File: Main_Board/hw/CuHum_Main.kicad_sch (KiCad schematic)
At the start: 50 parts, among them J1 Barrel_Jack_Switch_Pin3Ring, J101 Conn_01x07, J102 Conn_01x07, J103 Conn_01x07, J104 Conn_01x07, J105 Conn_01x07, J106 Conn_01x07, J107 Conn_01x07, J108 Conn_01x07, J109 Conn_01x07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

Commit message: Finish main board layout
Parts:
- J2: footprint CuHum_Main_footprints:TestPoints_1x04_P2.0 -> CuHum_Main_footprints:TestPoints_1x04_P2.54
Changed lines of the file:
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@@
       (effects (font (size 1.27 1.27)) (justify left) hide)
     )
-    (property "Footprint" "CuHum_Main_footprints:TestPoints_1x04_P2.0" (at 14.605 111.125 0)
+    (property "Footprint" "CuHum_Main_footprints:TestPoints_1x04_P2.54" (at 14.605 111.125 0)
       (effects (font (size 1.27 1.27)) hide)
     )

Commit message: (WIP) Main board layout & routing
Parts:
- J101, J102, J103, J104, J105, J106, J107, J108, J109, J110, J111, J112, J113, J114, J115: footprint Connector_PinHeader_2.54mm:PinHeader_1x07_P2.54mm_Vertical -> CuHum_Main_footprints:Unit_1x07_P2.54
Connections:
- net UNIT_CAP_01: now also U6.19 (LED7/ELE11); no longer U5.8 (ELE0)
- net UNIT_CAP_02: now also U5.10 (ELE2); no longer U5.9 (ELE1)
- net UNIT_CAP_03: now also U5.13 (LED1/ELE5); no longer U5.10 (ELE2)
- net UNIT_CAP_04: now also U5.18 (LED6/ELE10); no longer U5.11 (ELE3)
- net UNIT_CAP_05: now also U6.9 (ELE1); no longer U5.12 (LED0/ELE4)
- net UNIT_CAP_06: now also U6.13 (LED1/ELE5); no longer U5.13 (LED1/ELE5)
- net UNIT_CAP_07: now also U6.17 (LED5/ELE9); no longer U5.14 (LED2/ELE6)
- net UNIT_CAP_08: now also U5.9 (ELE1); no longer U5.15 (LED3/ELE7)
- net UNIT_CAP_09: now also U5.11 (ELE3); no longer U5.16 (LED4/ELE8)
- net UNIT_CAP_10: now also U5.16 (LED4/ELE8); no longer U5.17 (LED5/ELE9)
- net UNIT_CAP_11: now also U5.19 (LED7/ELE11); no longer U5.18 (LED6/ELE10)
- net UNIT_CAP_12: now also U6.10 (ELE2); no longer U5.19 (LED7/ELE11)
- net UNIT_CAP_13: now also U6.15 (LED3/ELE7); no longer U6.8 (ELE0)
- net UNIT_CAP_14: now also U6.18 (LED6/ELE10); no longer U6.9 (ELE1)
- net UNIT_CAP_15: now also U5.8 (ELE0); no longer U6.10 (ELE2)

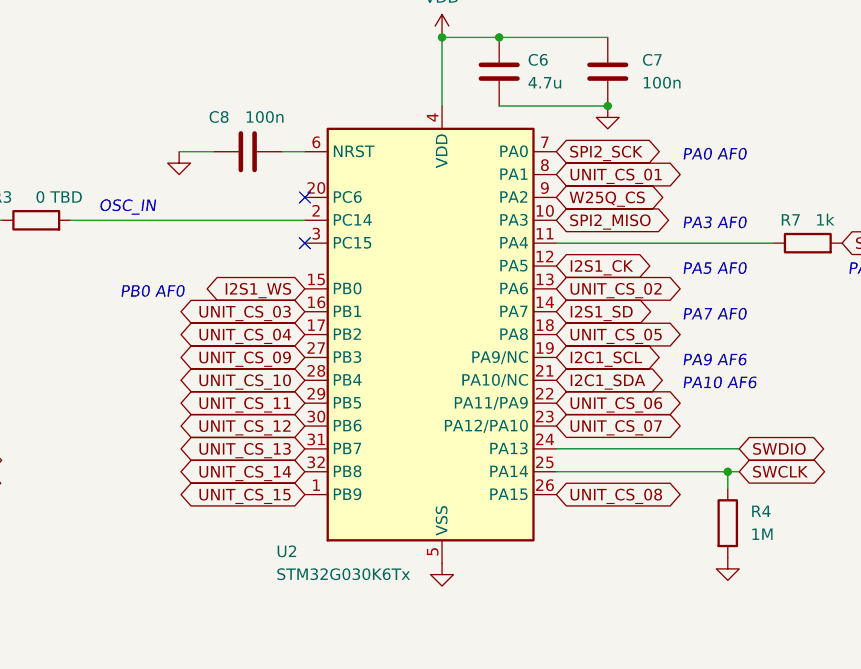
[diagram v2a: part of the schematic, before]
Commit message: Finish main board routing
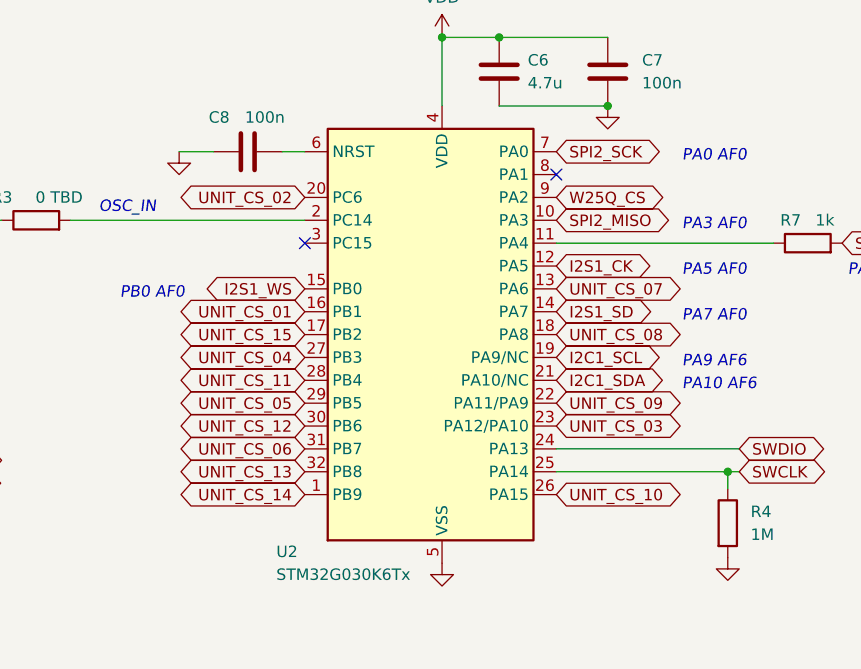
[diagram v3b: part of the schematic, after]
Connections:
- net UNIT_CS_01: now also U2.16 (PB1); no longer U2.8 (PA1)
- net UNIT_CS_02: now also U2.20 (PC6); no longer U2.13 (PA6)
- net UNIT_CS_03: now also U2.23 (PA12/PA10); no longer U2.16 (PB1)
- net UNIT_CS_04: now also U2.27 (PB3); no longer U2.17 (PB2)
- net UNIT_CS_05: now also U2.29 (PB5); no longer U2.18 (PA8)
- net UNIT_CS_06: now also U2.31 (PB7); no longer U2.22 (PA11/PA9)
- net UNIT_CS_07: now also U2.13 (PA6); no longer U2.23 (PA12/PA10)
- net UNIT_CS_08: now also U2.18 (PA8); no longer U2.26 (PA15)
- net UNIT_CS_09: now also U2.22 (PA11/PA9); no longer U2.27 (PB3)
- net UNIT_CS_10: now also U2.26 (PA15); no longer U2.28 (PB4)
- net UNIT_CS_11: now also U2.28 (PB4); no longer U2.29 (PB5)
- net UNIT_CS_13: now also U2.32 (PB8); no longer U2.31 (PB7)
- net UNIT_CS_14: now also U2.1 (PB9); no longer U2.32 (PB8)
- net UNIT_CS_15: now also U2.17 (PB2); no longer U2.1 (PB9)
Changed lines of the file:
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@@
   (no_connect (at 157.48 79.375))
   (no_connect (at 43.815 164.465))
+  (no_connect (at 90.805 81.915))
   (no_connect (at 62.865 89.535))
   (no_connect (at 250.19 88.9))
   (no_connect (at 137.795 161.925))
-  (no_connect (at 62.865 84.455))
   (no_connect (at 181.61 102.235))
   (no_connect (at 137.795 169.545))
@@
     )
   )
-  (global_label "UNIT_CS_01" (shape bidirectional) (at 90.805 81.915 0) (fields_autoplaced)
-    (effects (font (size 1.27 1.27)) (justify left))
-    (property "Intersheetrefs" "${INTERSHEET_REFS}" (at 105.9686 81.915 0)
-      (effects (font (size 1.27 1.27)) (justify left) hide)
-    )
-  )
   (global_label "UNIT_CAP_01" (shape bidirectional) (at 137.795 182.245 0) (fields_autoplaced)
     (effects (font (size 1.27 1.27)) (justify left))
@@
     )
   )
-  (global_label "UNIT_CS_11" (shape bidirectional) (at 62.865 107.315 180) (fields_autoplaced)
+  (global_label "UNIT_CS_05" (shape bidirectional) (at 62.865 107.315 180) (fields_autoplaced)
     (effects (font (size 1.27 1.27)) (justify right))
     (property "Intersheetrefs" "${INTERSHEET_REFS}" (at 47.7014 107.315 0)
@@
     )
   )
-  (global_label "UNIT_CS_04" (shape bidirectional) (at 62.865 99.695 180) (fields_autoplaced)
+  (global_label "UNIT_CS_15" (shape bidirectional) (at 62.865 99.695 180) (fields_autoplaced)
     (effects (font (size 1.27 1.27)) (justify right))
     (property "Intersheetrefs" "${INTERSHEET_REFS}" (at 47.7014 99.695 0)
@@
     )
   )
-  (global_label "UNIT_CS_14" (shape bidirectional) (at 62.865 114.935 180) (fields_autoplaced)
+  (global_label "UNIT_CS_13" (shape bidirectional) (at 62.865 114.935 180) (fields_autoplaced)
     (effects (font (size 1.27 1.27)) (justify right))
     (property "Intersheetrefs" "${INTERSHEET_REFS}" (at 47.7014 114.935 0)
@@
     )
   )
-  (global_label "UNIT_CS_09" (shape bidirectional) (at 62.865 102.235 180) (fields_autoplaced)
+  (global_label "UNIT_CS_04" (shape bidirectional) (at 62.865 102.235 180) (fields_autoplaced)
     (effects (font (size 1.27 1.27)) (justify right))
     (property "Intersheetrefs" "${INTERSHEET_REFS}" (at 47.7014 102.235 0)
@@
     )
   )
-  (global_label "UNIT_CS_13" (shape bidirectional) (at 62.865 112.395 180) (fields_autoplaced)
+  (global_label "UNIT_CS_06" (shape bidirectional) (at 62.865 112.395 180) (fields_autoplaced)
     (effects (font (size 1.27 1.27)) (justify right))
     (property "Intersheetrefs" "${INTERSHEET_REFS}" (at 47.7014 112.395 0)
@@
     )
   )
-  (global_label "UNIT_CS_05" (shape bidirectional) (at 90.805 99.695 0) (fields_autoplaced)
+  (global_label "UNIT_CS_08" (shape bidirectional) (at 90.805 99.695 0) (fields_autoplaced)
     (effects (font (size 1.27 1.27)) (justify left))
     (property "Intersheetrefs" "${INTERSHEET_REFS}" (at 105.9686 99.695 0)
@@
     )
   )
-  (global_label "UNIT_CS_15" (shape bidirectional) (at 62.865 117.475 180) (fields_autoplaced)
+  (global_label "UNIT_CS_14" (shape bidirectional) (at 62.865 117.475 180) (fields_autoplaced)
     (effects (font (size 1.27 1.27)) (justify right))
     (property "Intersheetrefs" "${INTERSHEET_REFS}" (at 47.7014 117.475 0)
@@
     )
   )
-  (global_label "UNIT_CS_03" (shape bidirectional) (at 62.865 97.155 180) (fields_autoplaced)
+  (global_label "UNIT_CS_01" (shape bidirectional) (at 62.865 97.155 180) (fields_autoplaced)
     (effects (font (size 1.27 1.27)) (justify right))
     (property "Intersheetrefs" "${INTERSHEET_REFS}" (at 47.7014 97.155 0)
@@
     )
   )
-  (global_label "UNIT_CS_10" (shape bidirectional) (at 62.865 104.775 180) (fields_autoplaced)
+  (global_label "UNIT_CS_11" (shape bidirectional) (at 62.865 104.775 180) (fields_autoplaced)
     (effects (font (size 1.27 1.27)) (justify right))
     (property "Intersheetrefs" "${INTERSHEET_REFS}" (at 47.7014 104.775 0)
@@
     )
   )
-  (global_label "UNIT_CS_02" (shape bidirectional) (at 90.805 94.615 0) (fields_autoplaced)
+  (global_label "UNIT_CS_07" (shape bidirectional) (at 90.805 94.615 0) (fields_autoplaced)
     (effects (font (size 1.27 1.27)) (justify left))
     (property "Intersheetrefs" "${INTERSHEET_REFS}" (at 105.9686 94.615 0)
@@
     )
   )
-  (global_label "UNIT_CS_07" (shape bidirectional) (at 90.805 109.855 0) (fields_autoplaced)
+  (global_label "UNIT_CS_03" (shape bidirectional) (at 90.805 109.855 0) (fields_autoplaced)
     (effects (font (size 1.27 1.27)) (justify left))
     (property "Intersheetrefs" "${INTERSHEET_REFS}" (at 105.9686 109.855 0)
@@
     )
   )
+  (global_label "UNIT_CS_02" (shape bidirectional) (at 62.865 84.455 180) (fields_autoplaced)
+    (effects (font (size 1.27 1.27)) (justify right))
+    (property "Intersheetrefs" "${INTERSHEET_REFS}" (at 47.7014 84.455 0)
+      (effects (font (size 1.27 1.27)) (justify right) hide)
+    )
+  )
   (global_label "UNIT_CS_13" (shape bidirectional) (at 137.795 243.205 180) (fields_autoplaced)
     (effects (font (size 1.27 1.27)) (justify right))
@@
     )
   )
-  (global_label "UNIT_CS_08" (shape bidirectional) (at 90.805 117.475 0) (fields_autoplaced)
+  (global_label "UNIT_CS_10" (shape bidirectional) (at 90.805 117.475 0) (fields_autoplaced)
     (effects (font (size 1.27 1.27)) (justify left))
     (property "Intersheetrefs" "${INTERSHEET_REFS}" (at 105.9686 117.475 0)
@@
     )
   )
-  (global_label "UNIT_CS_06" (shape bidirectional) (at 90.805 107.315 0) (fields_autoplaced)
+  (global_label "UNIT_CS_09" (shape bidirectional) (at 90.805 107.315 0) (fields_autoplaced)
     (effects (font (size 1.27 1.27)) (justify left))
     (property "Intersheetrefs" "${INTERSHEET_REFS}" (at 105.9686 107.315 0)
